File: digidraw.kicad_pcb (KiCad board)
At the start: 2 copper layers, 100 x 100 mm, 153 parts, among them CON1 SN49B12B, J1 USB_B_Micro, J10 USB_A, J11 Conn_02x05_Odd_Even, J12 Conn_01x03_Male, J13 Conn_01x04_Male, J2 Barrel_Jack, J3 Conn_02x05_Odd_Even, J4 Conn_01x06_Male, J5 Conn_01x05_Male, J6 Conn_01x04_Male, J7 Conn_01x15_Female, J8 Conn_01x04_Male, J9 Conn_01x05_Male, Q1 FDD5614P, SW1 SW_Push_Dual, SW2 SW_Push_Dual, SW3 SW_Push_Dual, SW4 SW_Push_Dual, SW5 SW_Push_Dual, SW6 SW_Push_Dual, U1 TPS63070RNMR, U2 LM117_TO3, U3 STM32F051R8T6, U4 CAT24C256, U5 STM32F407VGT6, U6 PCM5102, U7 STMPS2141STR, U8 LM117_TO3, U9 USBLC6-2SC6, Y1 8MHz, Y2 8MHz

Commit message: Get everything on board, use buck converter, chnage lm317 footprint
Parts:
- removed R47: 542, Resistor_SMD:R_0603_1608Metric
- removed R50: 330, Resistor_SMD:R_0603_1608Metric
- added L2: L_Small, Inductor_SMD:L_0603_1608Metric, F.Cu at (62.8, 71.0)
- C51: footprint Capacitor_SMD:C_0805_2012Metric -> Capacitor_SMD:C_0603_1608Metric
- C53: value 100n -> 10u; footprint Capacitor_SMD:C_0805_2012Metric -> Capacitor_SMD:C_0603_1608Metric
- C55: value 10u -> 22u
- U2: value LM117_TO3 -> V7803-1500R; footprint Package_TO_SOT_THT:TO-3 -> v7803:CONV_V7803-1500R
- U8: value LM117_TO3 -> LM317KCS; footprint Package_TO_SOT_THT:TO-3 -> lm317_ti:LM317KCS
- moved C24 138.5 mm to (104.0, 119.0)
- moved C22 138.1 mm to (100.0, 119.0)
- moved R36 136.4 mm to (102.0, 123.0)
- moved R11 133.3 mm to (61.8, 137.0)
- moved R12 133.3 mm to (57.8, 137.0)
- moved R32 130.8 mm to (96.0, 123.0)
- moved R26 130.1 mm to (110.0, 132.0)
- moved C8 128.5 mm to (62.8, 130.4)
- moved C9 128.5 mm to (58.3, 133.4)
- moved R13 127.7 mm to (62.9, 134.5)
- moved C7 127.6 mm to (58.3, 129.4)
- moved R27 127.5 mm to (110.0, 134.0)
- moved C36 123.7 mm to (119.0, 110.0)
- moved R14 123.5 mm to (85.3, 99.0)
- moved R15 123.0 mm to (85.3, 101.5)
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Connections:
- C53 pad 1: +3.3VA -> Net-(C53-Pad1)
- U2 pad 1: Net-(R47-Pad1) -> Net-(C48-Pad1)
- U2 pad 2: Net-(C48-Pad1) -> GND
- U2 pad 3: +3.3VA -> Net-(C53-Pad1)
- U8 pad 2: Net-(C48-Pad1) -> +3.3VDAC
- U8 pad 3: +3.3VDAC -> Net-(C48-Pad1)

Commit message: Decent layout at first glance
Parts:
- moved D5 62.4 mm to (129.0, 78.0)
- moved R28 62.4 mm to (133.0, 78.0), turned to 180 degrees
- moved D4 58.7 mm to (129.0, 80.0)
- moved R27 58.7 mm to (133.0, 80.0), turned to 180 degrees
- moved D3 55.0 mm to (129.0, 82.0)
- moved R26 55.0 mm to (133.0, 82.0), turned to 180 degrees
- moved D2 51.4 mm to (129.0, 84.0)
- moved R25 51.4 mm to (133.0, 84.0), turned to 180 degrees
- moved J11 34.7 mm to (110.0, 62.0), turned to 270 degrees
- moved R31 33.1 mm to (92.0, 96.0), turned to 90 degrees
- moved C52 31.1 mm to (120.0, 68.0)
- moved C54 31.1 mm to (128.0, 73.0)
- moved C56 31.1 mm to (127.8, 71.0)
- moved R48 31.1 mm to (118.0, 74.0)
- moved R51 31.1 mm to (120.0, 74.0)
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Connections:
- C40 pad 2: +3.3VADC -> +3.3VDAC
- C42 pad 2: +3.3VADC -> +3.3VDAC
- U6 pad 8: +3.3VADC -> +3.3VDAC

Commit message: Replace components
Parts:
- J7: value Conn_01x15_Female -> Conn_01x09_Male; footprint Connector_PinSocket_2.54mm:PinSocket_1x15_P2.54mm_Vertical -> Connector_PinHeader_2.54mm:PinHeader_1x09_P2.54mm_Vertical
- J8: footprint Connector_PinSocket_2.54mm:PinSocket_1x04_P2.54mm_Vertical -> Connector_PinHeader_2.54mm:PinHeader_1x04_P2.54mm_Vertical
- J9: footprint Connector_PinSocket_2.54mm:PinSocket_1x05_P2.54mm_Vertical -> Connector_PinHeader_2.54mm:PinHeader_1x05_P2.54mm_Vertical
- moved C1 108.6 mm to (151.0, 91.0)
- moved C4 108.6 mm to (175.0, 88.0)
- moved C5 108.6 mm to (172.0, 93.0)
- moved C6 108.6 mm to (177.0, 94.0)
- moved D1 108.6 mm to (151.0, 89.0)
- moved D6 108.6 mm to (157.0, 93.0)
- moved F1 108.6 mm to (165.0, 83.0)
- moved L1 108.6 mm to (178.0, 91.0)
- moved Q1 108.6 mm to (157.0, 85.0)
- moved R1 108.6 mm to (154.0, 93.0)
- moved R10 108.6 mm to (169.0, 92.0)
- moved R2 108.6 mm to (169.0, 89.0)
- moved R7 108.6 mm to (174.0, 98.0)
- moved R9 108.6 mm to (174.0, 100.0)
- moved U1 108.6 mm to (175.4, 91.0)
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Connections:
- J4 pad 2: /user_io/RA8875_MISO -> /user_io/RA8875_NSS
- J4 pad 4: /user_io/RA8875_SCK -> /user_io/RA8875_MISO
- J4 pad 5: /user_io/RA8875_NSS -> /user_io/RA8875_SCK
- J7 pad 3: Net-(J7-Pad3) -> /user_io/RA8875_SCK
- J7 pad 4: Net-(J7-Pad4) -> /user_io/RA8875_MISO
- J7 pad 5: /user_io/RA8875_SCK -> /user_io/RA8875_MOSI
- J7 pad 6: /user_io/RA8875_MISO -> /user_io/RA8875_NSS
- J7 pad 7: /user_io/RA8875_MOSI -> /user_io/RA8875_NRST
- J7 pad 8: /user_io/RA8875_NSS -> /user_io/RA8875_WAIT
- J7 pad 9: /user_io/RA8875_NRST -> /user_io/RA8875_INT
- J9 pad 2: /midi_dac/I2S_SD -> /midi_dac/I2S_WS
- J9 pad 3: /midi_dac/I2S_CK -> /midi_dac/I2S_SD
- J9 pad 4: /midi_dac/I2S_WS -> /midi_dac/I2S_CK
- U5 pad 15: /midi_dac/USB_VBUS_EN -> Net-(U5-Pad15)
- U5 pad 18: Net-(R31-Pad2) -> Net-(U5-Pad18)
- U5 pad 23: /midi_dac/GPIO_EXTI0 -> /midi_dac/UART4_TX
- U5 pad 31: Net-(U5-Pad31) -> /midi_dac/SPI_INT
- U5 pad 54: Net-(U5-Pad54) -> Net-(R31-Pad2)
- U5 pad 69: Net-(U5-Pad69) -> /midi_dac/USB_VBUS_EN
- U5 pad 78: /midi_dac/UART4_TX -> Net-(U5-Pad78)
- U5 pad 90: /midi_dac/SPI_INT -> Net-(U5-Pad90)
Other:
- board size 100 x 100 mm -> 140 x 100 mm

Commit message: Huge progress on routing
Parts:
- removed D4: ORA_LED, LED_SMD:LED_0603_1608Metric
- removed D5: RED_LED, LED_SMD:LED_0603_1608Metric
- removed R27, R28: 75, Resistor_SMD:R_0603_1608Metric
- D2: value BLUE_LED -> LED
- D3: value GREEN_LED -> LED
- J11, J3: value Conn_02x05_Odd_Even -> Conn_02x10_Odd_Even; footprint Connector_PinHeader_2.54mm:PinHeader_2x05_P2.54mm_Vertical -> Connector_PinHeader_1.27mm:PinHeader_2x10_P1.27mm_Vertical
- R25: value 75 -> 208
- R26: value 75 -> 100
- moved R26 87.1 mm to (145.6, 116.9)
- moved D3 84.4 mm to (145.5, 112.9)
- moved R25 78.9 mm to (144.8, 95.8), turned to 0 degrees
- moved D2 74.5 mm to (140.8, 95.8), turned to 180 degrees
- moved R36 39.2 mm to (137.4, 119.0), turned to 270 degrees
- moved C24 36.9 mm to (135.4, 119.0), turned to 90 degrees
- moved R49 30.2 mm to (138.3, 99.9)
- moved SW6 29.4 mm to (128.4, 119.0), turned to 180 degrees
- moved R22 27.8 mm to (90.2, 144.9), turned to 0 degrees
- moved J13 25.3 mm to (85.3, 121.2), turned to 90 degrees
- moved R17 18.7 mm to (73.5, 146.7), turned to 270 degrees
- moved J3 12.4 mm to (86.4, 160.2), turned to 180 degrees
- moved C51 9.56 mm to (159.5, 96.1), turned to 180 degrees
- moved C57 8.32 mm to (84.3, 85.0), turned to 270 degrees
- moved R34 4.66 mm to (82.4, 81.0)
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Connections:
- D2 pad 1: /midi_dac/GPIO_OUTPUT_D12 -> Net-(D2-Pad1)
- D2 pad 2: Net-(D2-Pad2) -> +5V
- D3 pad 1: /midi_dac/GPIO_OUTPUT_D13 -> Net-(D3-Pad1)
- D3 pad 2: Net-(D3-Pad2) -> +3.3VA
- J11 pad 10: /midi_dac/NRST -> GND
- J11 pad 2: /midi_dac/SWDIO -> Net-(J11-Pad2)
- J11 pad 3: GND -> Net-(J11-Pad3)
- J11 pad 4: /midi_dac/SWCLK -> GND
- J11 pad 5: GND -> Net-(J11-Pad5)
- J11 pad 6: /midi_dac/SWO -> GND
- J11 pad 7: Net-(J11-Pad7) -> /midi_dac/SWDIO
- J11 pad 8: Net-(J11-Pad8) -> GND
- J11 pad 9: GND -> /midi_dac/SWCLK
- J3 pad 10: /user_io/NRST -> GND
- J3 pad 2: /user_io/SWDIO -> GND
- J3 pad 3: GND -> Net-(J3-Pad3)
- J3 pad 4: /user_io/SWCLK -> GND
- J3 pad 5: GND -> Net-(J3-Pad5)
- J3 pad 6: Net-(J3-Pad6) -> GND
- J3 pad 7: Net-(J3-Pad7) -> /user_io/SWDIO
- J3 pad 8: Net-(J3-Pad8) -> GND
- J3 pad 9: GND -> /user_io/SWCLK
- R25 pad 1: +3.3VA -> Net-(D2-Pad1)
- R25 pad 2: Net-(D2-Pad2) -> GND
- R26 pad 1: +3.3VA -> Net-(D3-Pad1)
- R26 pad 2: Net-(D3-Pad2) -> GND
- U5 pad 59: /midi_dac/GPIO_OUTPUT_D12 -> Net-(U5-Pad59)
- U5 pad 60: /midi_dac/GPIO_OUTPUT_D13 -> Net-(U5-Pad60)
- U5 pad 61: /midi_dac/GPIO_OUTPUT_D14 -> Net-(U5-Pad61)
- U5 pad 62: /midi_dac/GPIO_OUTPUT_D15 -> Net-(U5-Pad62)
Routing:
- net +3.3VA: track 0.00 -> 620.1 mm
- net GND: track 0.00 -> 207.4 mm, vias 0 -> 114
- net Net-(C48-Pad1): track 0.00 -> 108.5 mm
- net /midi_dac/SPI_NSS: track 0.00 -> 62.4 mm
- net +5V: track 0.00 -> 62.0 mm
- net /midi_dac/SPI_SCK: track 0.00 -> 59.4 mm, vias 0 -> 2
- net /midi_dac/SPI_MOSI: track 0.00 -> 58.2 mm, vias 0 -> 2
- net /midi_dac/BOOT1: track 0.00 -> 53.9 mm, vias 0 -> 2
- net /user_io/NRST: track 0.00 -> 53.4 mm, vias 0 -> 2
- net /user_io/RA8875_NSS: track 0.00 -> 51.0 mm
- net /user_io/RA8875_NRST: track 0.00 -> 45.3 mm
- net /midi_dac/NRST: track 0.00 -> 44.6 mm, vias 0 -> 2
- net /midi_dac/ANALOG_L: track 0.00 -> 43.4 mm
- net +3.3VDAC: track 0.00 -> 43.2 mm
- net /user_io/RA8875_SCK: track 0.00 -> 35.7 mm
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- added copper zone on B.Cu, net GND
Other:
- net class Power added: clearance 0.2, trace_width 0.5, via_dia 0.8, via_drill 0.4
- rule trace_min: 0.2 -> 0.127
- rule via_min_size: 0.4 -> 0.6

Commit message: Finish initial layout
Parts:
- removed SW1, SW2, SW3, SW4, SW5, SW6: SW_Push_Dual, Button_Switch_SMD:SW_SPST_EVPBF
- added J14: Conn_01x02_Male, Connector_PinHeader_2.54mm:PinHeader_1x02_P2.54mm_Vertical, F.Cu at (117.5, 154.9)
- added J15: Conn_01x02_Male, Connector_PinHeader_2.54mm:PinHeader_1x02_P2.54mm_Vertical, F.Cu at (122.0, 134.6)
- added J16: Conn_01x02_Male, Connector_PinHeader_2.54mm:PinHeader_1x02_P2.54mm_Vertical, F.Cu at (65.9, 116.9)
- added J17: Conn_01x02_Male, Connector_PinHeader_2.54mm:PinHeader_1x02_P2.54mm_Vertical, F.Cu at (73.8, 123.6)
- added J18: Conn_01x02_Male, Connector_PinHeader_2.54mm:PinHeader_1x02_P2.54mm_Vertical, F.Cu at (132.4, 117.9)
- added J19: Conn_01x02_Male, Connector_PinHeader_2.54mm:PinHeader_1x02_P2.54mm_Vertical, F.Cu at (127.1, 146.9)
- added R27: 300k, Resistor_SMD:R_0603_1608Metric, F.Cu at (91.1, 86.3)
- added R28: 200k, Resistor_SMD:R_0603_1608Metric, F.Cu at (94.2, 86.3)
- J11, J3: value Conn_02x10_Odd_Even -> Conn_02x05_Odd_Even; footprint Connector_PinHeader_1.27mm:PinHeader_2x10_P1.27mm_Vertical -> Connector_PinHeader_1.27mm:PinHeader_2x05_P1.27mm_Vertical
- moved U2 28.4 mm to (172.0, 121.0), turned to 270 degrees
- moved R14 24.8 mm to (98.3, 121.1), turned to 180 degrees
- moved R20 20.2 mm to (85.0, 142.3), turned to 180 degrees
- moved R18 17.3 mm to (85.0, 140.0), turned to 180 degrees
- moved R33 14.5 mm to (75.0, 118.5), turned to 0 degrees
- moved R48 12.4 mm to (137.4, 106.3), turned to 180 degrees
- moved R51 11.8 mm to (136.6, 104.0)
- moved C23 10.5 mm to (75.0, 120.5), turned to 180 degrees
- moved J3 10.5 mm to (84.0, 150.0), turned to 0 degrees
- moved C53 9.85 mm to (170.0, 108.0), turned to 0 degrees
- moved J5 8.85 mm to (115.5, 125.8), turned to 180 degrees
- moved L2 7.60 mm to (167.4, 107.2), turned to 270 degrees
- moved C50 6.32 mm to (174.0, 108.0), turned to 180 degrees
- moved C55 5.66 mm to (170.0, 106.3), turned to 0 degrees
- moved R37 5.05 mm to (100.0, 87.0)
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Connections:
- C10 pad 1: +3.3VA -> +3V3
- C12 pad 1: +3.3VA -> +3V3
- C14 pad 1: +3.3VA -> +3V3
- C15 pad 1: +3.3VA -> +3V3
- C16 pad 1: +3.3VA -> +3V3
- C17 pad 1: +3.3VA -> +3V3
- C18 pad 1: +3.3VA -> +3V3
- C19 pad 1: +3.3VA -> +3V3
- C23 pad 1: +3.3VA -> +3V3
- C24 pad 1: +3.3VA -> +3V3
- C25 pad 1: +3.3VA -> +3V3
- C26 pad 1: +3.3VA -> +3V3
- C27 pad 1: +3.3VA -> +3V3
- C29 pad 1: +3.3VA -> +3V3
- C31 pad 1: +3.3VA -> +3V3
- C32 pad 1: +3.3VA -> +3V3
- C34 pad 1: +3.3VA -> +3V3
- C35 pad 1: +3.3VA -> +3V3
- C37 pad 1: +3.3VA -> +3V3
- C38 pad 1: +3.3VA -> +3V3
- C41 pad 1: +3.3VA -> +3V3
- C43 pad 1: +3.3VA -> +3V3
- C44 pad 1: /midi_dac/USB_POWER -> /midi_dac/USB_FS_VBUS
- C55 pad 1: +3.3VA -> +3V3
- C7 pad 2: +3.3VA -> +3V3
- C9 pad 2: +3.3VA -> +3V3
- D3 pad 2: +3.3VA -> +3V3
- J10 pad 1: /midi_dac/USB_POWER -> /midi_dac/USB_FS_VBUS
- J11 pad 1: +3.3VA -> +3V3
- J11 pad 10: GND -> /midi_dac/NRST
- J11 pad 2: Net-(J11-Pad2) -> /midi_dac/SWDIO
- J11 pad 3: Net-(J11-Pad3) -> GND
- J11 pad 4: GND -> /midi_dac/SWCLK
- J11 pad 5: Net-(J11-Pad5) -> GND
- J11 pad 6: GND -> /midi_dac/SWO
- J11 pad 7: /midi_dac/SWDIO -> Net-(J11-Pad7)
- J11 pad 8: GND -> Net-(J11-Pad8)
- J11 pad 9: /midi_dac/SWCLK -> GND
- J13 pad 4: +3.3VA -> +3V3
- J3 pad 1: +3.3VA -> +3V3
- J3 pad 10: GND -> /user_io/NRST
- J3 pad 2: GND -> /user_io/SWDIO
- J3 pad 3: Net-(J3-Pad3) -> GND
- J3 pad 4: GND -> /user_io/SWCLK
- J3 pad 5: Net-(J3-Pad5) -> GND
- J3 pad 6: GND -> Net-(J3-Pad6)
- J3 pad 7: /user_io/SWDIO -> Net-(J3-Pad7)
- J3 pad 8: GND -> Net-(J3-Pad8)
- J3 pad 9: /user_io/SWCLK -> GND
- J4 pad 6: +3.3VA -> +3V3
- J5 pad 5: +3.3VA -> +3V3
- J6 pad 4: +3.3VA -> +3V3
- J7 pad 1: +3.3VA -> +3V3
- J8 pad 4: +3.3VA -> +3V3
- J9 pad 5: +3.3VA -> Net-(J9-Pad5)
- L2 pad 1: +3.3VA -> +3V3
- R13 pad 1: +3.3VA -> +3V3
- R15 pad 2: +3.3VA -> +3V3
- R21 pad 1: +3.3VA -> +3V3
- R22 pad 1: +3.3VA -> +3V3
- R23 pad 1: +3.3VA -> +3V3
- R24 pad 1: +3.3VA -> +3V3
- R32 pad 2: +3.3VA -> +3V3
- R43 pad 1: +3.3VA -> +3V3
- R46 pad 2: +3.3VA -> +3V3
- U3 pad 1: +3.3VA -> +3V3
- U3 pad 13: +3.3VA -> +3V3
- U3 pad 26: /user_io/RA8875_INT -> Net-(U3-Pad26)
- U3 pad 27: /user_io/RA8875_WAIT -> Net-(U3-Pad27)
- U3 pad 28: Net-(U3-Pad28) -> /midi_dac/SPI_INT
- U3 pad 32: +3.3VA -> +3V3
- U3 pad 37: Net-(U3-Pad37) -> /user_io/RA8875_WAIT
- U3 pad 38: Net-(U3-Pad38) -> /user_io/RA8875_INT
- U3 pad 39: /user_io/RA8875_NRST -> Net-(U3-Pad39)
- U3 pad 41: /midi_dac/SPI_INT -> /user_io/RA8875_NRST
- U3 pad 64: +3.3VA -> +3V3
- U4 pad 8: +3.3VA -> +3V3
- U5 pad 100: +3.3VA -> +3V3
- U5 pad 11: +3.3VA -> +3V3
- U5 pad 19: +3.3VA -> +3V3
- U5 pad 21: +3.3VA -> +3V3
- U5 pad 22: +3.3VA -> +3V3
- U5 pad 28: +3.3VA -> +3V3
- U5 pad 34: /midi_dac/SOFT_MUTE -> Net-(U5-Pad34)
- U5 pad 45: Net-(U5-Pad45) -> /midi_dac/SOFT_MUTE
- U5 pad 50: +3.3VA -> +3V3
- U5 pad 6: +3.3VA -> +3V3
- U5 pad 75: +3.3VA -> +3V3
- U6 pad 1: +3.3VA -> +3V3
- U6 pad 20: +3.3VA -> +3V3
- U7 pad 1: /midi_dac/USB_POWER -> /midi_dac/USB_FS_VBUS
- U7 pad 5: /midi_dac/USB_FS_VBUS -> +5V
- Y2 pad 4: +3.3VA -> +3V3
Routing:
- net +3V3: track 0.00 -> 659.4 mm, vias 0 -> 8
- net +3.3VA: track 620.1 -> 0.00 mm
- net +5V: track 62.0 -> 151.9 mm
- net /user_io/NRST: track 53.4 -> 85.6 mm
- net /user_io/RA8875_INT: track 6.81 -> 35.4 mm
- net /user_io/RA8875_WAIT: track 6.74 -> 35.0 mm
- net /midi_dac/SPI_INT: track 11.2 -> 37.8 mm, vias 0 -> 2
- net Net-(C48-Pad1): track 108.5 -> 90.6 mm
- net /midi_dac/USB_FS_VBUS: track 17.7 -> 35.3 mm
- net /midi_dac/BOOT0: track 12.2 -> 28.9 mm, vias 0 -> 2
- net /midi_dac/USB_POWER: track 13.8 -> 0.00 mm
- net /midi_dac/SWO: track 23.1 -> 11.5 mm, vias 2 -> 0
- net /midi_dac/SWDIO: track 28.8 -> 18.0 mm, vias 2 -> 0
- net /midi_dac/SWCLK: track 22.2 -> 12.8 mm, vias 2 -> 0
- net Net-(R48-Pad1): track 13.4 -> 4.95 mm
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- added copper zone on F.Cu, net GND
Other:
- board text added: "Team 23 Digidraw Synth Cooper Campbell, Nicholas O'Donnel, Nick Shirrell Revision 1"

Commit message: Add gerber files
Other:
- board text added: "ECE49022, Team 23 Digidraw Synth Cooper Campbell, Nicholas O'Donnel, Nick Shirrell Revision 1"
- board text removed: "Team 23 Digidraw Synth Cooper Campbell, Nicholas O'Donnel, Nick Shirrell Revision 1"

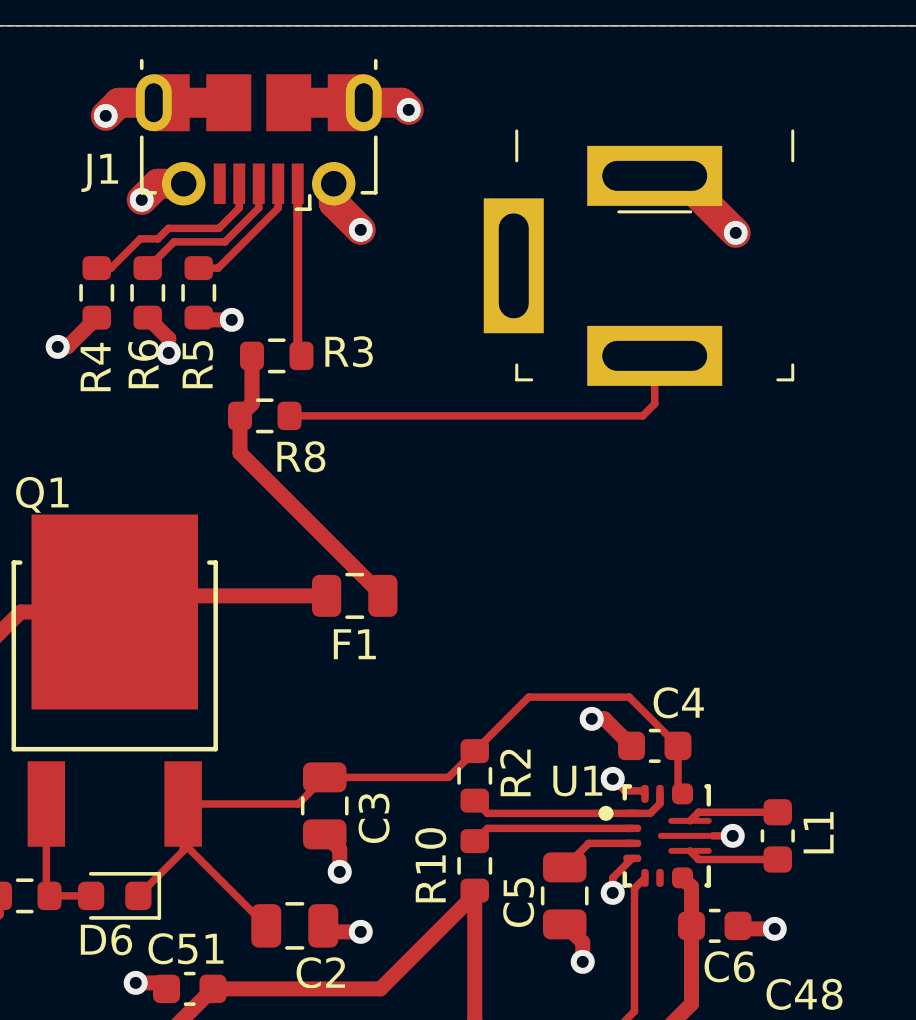
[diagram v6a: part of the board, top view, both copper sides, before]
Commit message: Documentation for submission
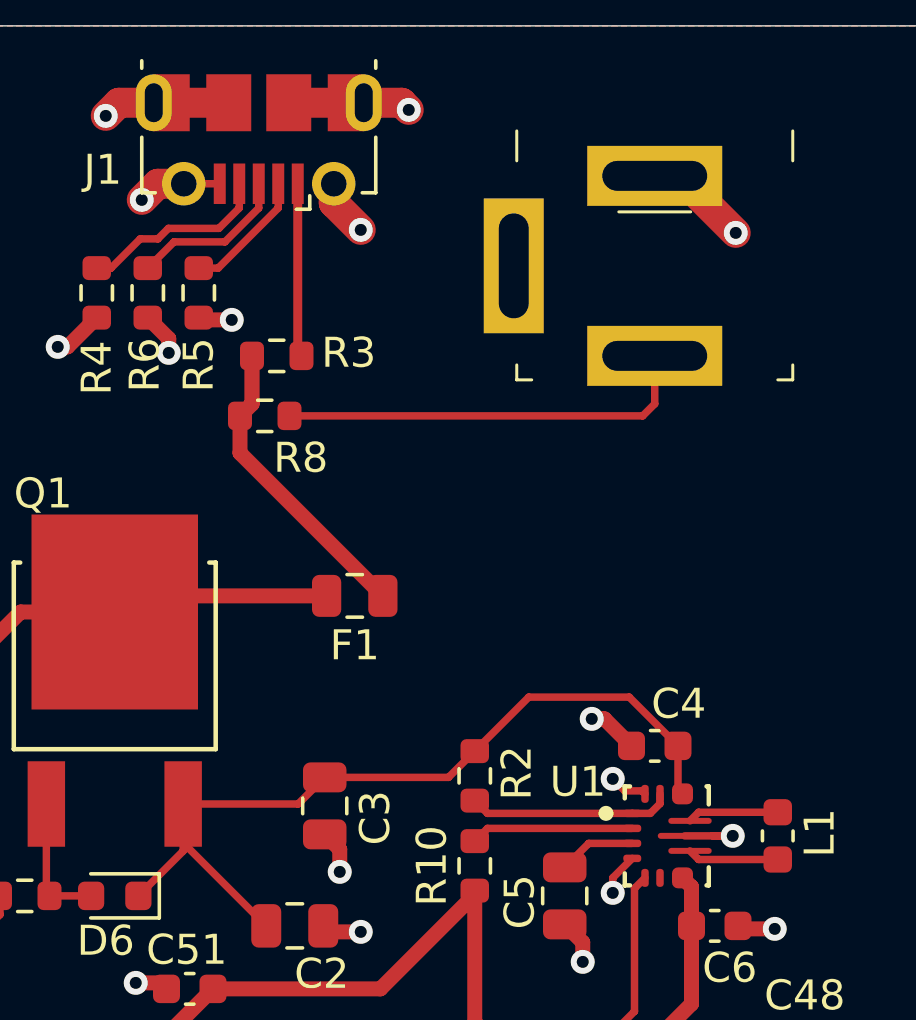
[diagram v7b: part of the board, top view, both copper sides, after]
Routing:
- net GND: track 207.6 -> 210.4 mm

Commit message: PCB changes
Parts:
- removed F1: 3, Fuse:Fuse_0805_2012Metric
- added R47: 0, Resistor_SMD:R_0603_1608Metric, F.Cu at (79.2, 70.8)
- added R50: 47k, Resistor_SMD:R_0603_1608Metric, F.Cu at (87.8, 88.1)
- added R53: 97k, Resistor_SMD:R_0603_1608Metric, F.Cu at (85.0, 89.6)
- J13: value Conn_01x04_Male -> Conn_01x03_Male; footprint Connector_PinHeader_2.54mm:PinHeader_1x04_P2.54mm_Vertical -> Connector_PinHeader_2.54mm:PinHeader_1x03_P2.54mm_Vertical
- J9: value Conn_01x05_Male -> Conn_01x04_Male; footprint Connector_PinHeader_2.54mm:PinHeader_1x05_P2.54mm_Vertical -> Connector_PinHeader_2.54mm:PinHeader_1x04_P2.54mm_Vertical
- L1: footprint Inductor_SMD:L_0603_1608Metric -> custom_fp:InductorWEPD
- L2: value L_Small -> 10u
- moved J9 16.3 mm to (101.4, 89.8), turned to 0 degrees
- moved R31 11.0 mm to (89.1, 90.7), turned to 270 degrees
- moved L1 8.83 mm to (187.8, 89.5), turned to 0 degrees
- moved R30 8.51 mm to (91.5, 91.4)
- moved C57 7.10 mm to (84.1, 77.9), turned to 90 degrees
- moved R29 6.95 mm to (94.7, 97.5)
- moved J13 6.31 mm to (90.1, 117.1)
- moved R9 6.26 mm to (171.9, 94.1), turned to 180 degrees
- moved C18 4.19 mm to (96.3, 160.5)
- moved R7 4.05 mm to (175.1, 94.1)
- moved C31 3.72 mm to (88.6, 111.5), turned to 180 degrees
- moved R34 3.62 mm to (85.6, 82.7)
- moved U9 2.83 mm to (87.0, 79.0)
- moved R35 1.80 mm to (87.4, 82.7)
- moved R36 1.80 mm to (137.5, 117.2), turned to 90 degrees
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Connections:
- C1 pad 1: Net-(C1-Pad1) -> /VIN
- C44 pad 1: /midi_dac/USB_FS_VBUS -> /midi_dac/USB_POWER
- D1 pad 1: Net-(C1-Pad1) -> /VIN
- J10 pad 1: /midi_dac/USB_FS_VBUS -> /midi_dac/USB_POWER
- J10 pad 5: GND -> Net-(J10-Pad5)
- J9 pad 2: /midi_dac/I2S_WS -> /midi_dac/I2S_SD
- J9 pad 3: /midi_dac/I2S_SD -> /midi_dac/I2S_WS
- Q1 pad 4: Net-(C1-Pad1) -> /VIN
- R34 pad 2: /midi_dac/USB_DP -> Net-(R34-Pad2)
- R35 pad 2: /midi_dac/USB_DM -> Net-(R35-Pad2)
- U5 pad 45: /midi_dac/SOFT_MUTE -> Net-(U5-Pad45)
- U5 pad 55: Net-(U5-Pad55) -> /midi_dac/SOFT_MUTE
- U5 pad 67: Net-(U5-Pad67) -> /midi_dac/USB_VBUS_EN
- U5 pad 69: /midi_dac/USB_VBUS_EN -> Net-(U5-Pad69)
- U6 pad 1: +3V3 -> +3.3VDAC
- U7 pad 1: /midi_dac/USB_FS_VBUS -> /midi_dac/USB_POWER
- U9 pad 4: /midi_dac/USB_FS_DP -> Net-(R34-Pad2)
- U9 pad 6: /midi_dac/USB_FS_DM -> Net-(R35-Pad2)
- Y2 pad 4: +3V3 -> GND
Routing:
- net +3V3: track 659.4 -> 607.5 mm
- net /midi_dac/USB_FS_VBUS: track 35.3 -> 8.43 mm
- net GND: track 210.4 -> 236.6 mm, vias 124 -> 110
- net /midi_dac/USB_POWER: track 0.00 -> 25.4 mm
- net +5V: track 151.9 -> 133.0 mm
- net +3.3VDAC: track 36.1 -> 53.3 mm
- net Net-(J10-Pad5): track 0.00 -> 16.3 mm
- net Net-(C1-Pad1): track 15.3 -> 0.00 mm
- net Net-(C48-Pad1): track 90.6 -> 104.2 mm
- net Net-(L1-Pad2): track 3.04 -> 14.1 mm
- net Net-(R31-Pad2): track 13.0 -> 2.05 mm
- net Net-(L1-Pad1): track 3.04 -> 12.8 mm
- net /midi_dac/I2S_SD: track 25.2 -> 34.3 mm
- net /VIN: track 10.1 -> 18.4 mm
- net Net-(R30-Pad2): track 10.1 -> 2.20 mm
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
